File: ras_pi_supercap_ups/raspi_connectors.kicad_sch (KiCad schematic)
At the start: 2 parts

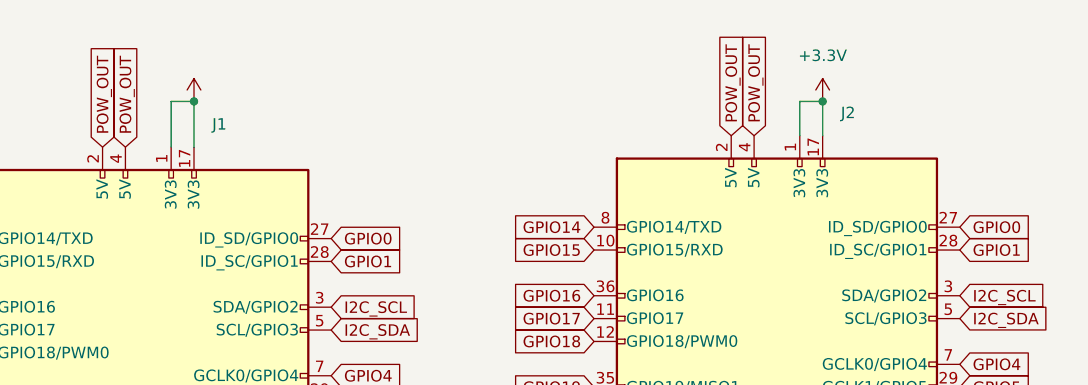
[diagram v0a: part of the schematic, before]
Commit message: added 3d model
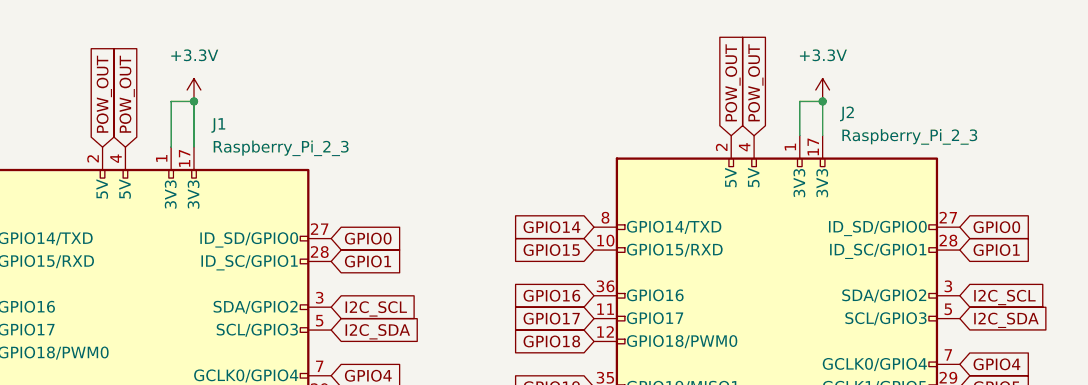
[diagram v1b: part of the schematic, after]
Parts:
- J1, J2: value (none) -> Raspberry_Pi_2_3
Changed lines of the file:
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@@
       (effects (font (size 1.27 1.27)) hide)
     )
-    (property "Value" "" (id 1) (at 66.04 21.59 0))
+    (property "Value" "+3.3V" (id 1) (at 66.04 21.59 0))
     (property "Footprint" "" (id 2) (at 66.04 26.67 0)
       (effects (font (size 1.27 1.27)) hide)
@@
       (effects (font (size 1.27 1.27)) (justify left))
     )
-    (property "Value" "" (id 1) (at 137.9094 30.48 0)
+    (property "Value" "Raspberry_Pi_2_3" (id 1) (at 137.9094 30.48 0)
       (effects (font (size 1.27 1.27)) (justify left))
     )
@@
       (effects (font (size 1.27 1.27)) (justify left))
     )
-    (property "Value" "" (id 1) (at 68.0594 31.75 0)
+    (property "Value" "Raspberry_Pi_2_3" (id 1) (at 68.0594 31.75 0)
       (effects (font (size 1.27 1.27)) (justify left))
     )

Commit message: As ordered v0.9
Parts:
- J1, J2: footprint (none) -> Connector_PinSocket_2.54mm:PinSocket_2x20_P2.54mm_Vertical; LCSC (none) -> DNP
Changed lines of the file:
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@@
   (junction (at 135.89 100.33) (diameter 0) (color 0 0 0 0)
   )
+  (junction (at 133.35 26.67) (diameter 0) (color 0 0 0 0)
+  )
   (junction (at 63.5 101.6) (diameter 0) (color 0 0 0 0)
   )
@@
     (stroke (width 0) (type default) (color 0 0 0 0))
   )
+  (wire (pts (xy 105.41 24.13) (xy 105.41 22.86))
+    (stroke (width 0) (type default) (color 0 0 0 0))
+  )
   (wire (pts (xy 55.88 101.6) (xy 58.42 101.6))
     (stroke (width 0) (type default) (color 0 0 0 0))
@@
     (stroke (width 0) (type default) (color 0 0 0 0))
   )
+  (wire (pts (xy 100.33 24.13) (xy 105.41 24.13))
+    (stroke (width 0) (type default) (color 0 0 0 0))
+  )
   (wire (pts (xy 123.19 100.33) (xy 125.73 100.33))
     (stroke (width 0) (type default) (color 0 0 0 0))
@@
     (property "Intersheet References" "${INTERSHEET_REFS}" (id 0) (at 91.3131 51.9906 0)
       (effects (font (size 1.27 1.27)) (justify left) hide)
+    )
+  )
+  (global_label "POW_OUT" (shape input) (at 100.33 24.13 180) (fields_autoplaced)
+    (effects (font (size 1.27 1.27)) (justify right))
+    (property "Intersheet References" "${INTERSHEET_REFS}" (id 0) (at 89.2688 24.2094 0)
+      (effects (font (size 1.27 1.27)) (justify right) hide)
     )
   )
@@
   )
   (symbol (lib_id "power:+3.3V") (at 135.89 26.67 0) (unit 1)
-    (in_bom yes) (on_board yes) (fields_autoplaced)
+    (in_bom yes) (on_board yes)
     (property "Reference" "#PWR035" (id 0) (at 135.89 30.48 0)
       (effects (font (size 1.27 1.27)) hide)
     )
-    (property "Value" "+3.3V" (id 1) (at 135.89 21.59 0))
+    (property "Value" "+3.3V" (id 1) (at 135.89 20.32 90))
     (property "Footprint" "" (id 2) (at 135.89 26.67 0)
       (effects (font (size 1.27 1.27)) hide)
@@
       (effects (font (size 1.27 1.27)) (justify left))
     )
-    (property "Footprint" "" (id 2) (at 130.81 63.5 0)
+    (property "Footprint" "Connector_PinSocket_2.54mm:PinSocket_2x20_P2.54mm_Vertical" (id 2) (at 130.81 63.5 0)
       (effects (font (size 1.27 1.27)) hide)
     )
     (property "Datasheet" "https://www.raspberrypi.org/documentation/hardware/raspberrypi/schematics/rpi_SCH_3bplus_1p0_reduced.pdf" (id 3) (at 130.81 63.5 0)
+      (effects (font (size 1.27 1.27)) hide)
+    )
+    (property "LCSC" "DNP" (id 4) (at 130.81 63.5 0)
       (effects (font (size 1.27 1.27)) hide)
     )
@@
     (pin "9")
   )
+  (symbol (lib_id "power:PWR_FLAG") (at 133.35 26.67 0) (unit 1)
+    (in_bom yes) (on_board yes)
+    (property "Reference" "#FLG0101" (id 0) (at 133.35 24.765 0)
+      (effects (font (size 1.27 1.27)) hide)
+    )
+    (property "Value" "PWR_FLAG" (id 1) (at 133.35 19.05 90))
+    (property "Footprint" "" (id 2) (at 133.35 26.67 0)
+      (effects (font (size 1.27 1.27)) hide)
+    )
+    (property "Datasheet" "~" (id 3) (at 133.35 26.67 0)
+      (effects (font (size 1.27 1.27)) hide)
+    )
+    (pin "1")
+  )
+  (symbol (lib_id "power:PWR_FLAG") (at 105.41 22.86 0) (unit 1)
+    (in_bom yes) (on_board yes)
+    (property "Reference" "#FLG0102" (id 0) (at 105.41 20.955 0)
+      (effects (font (size 1.27 1.27)) hide)
+    )
+    (property "Value" "PWR_FLAG" (id 1) (at 105.41 19.05 0))
+    (property "Footprint" "" (id 2) (at 105.41 22.86 0)
+      (effects (font (size 1.27 1.27)) hide)
+    )
+    (property "Datasheet" "~" (id 3) (at 105.41 22.86 0)
+      (effects (font (size 1.27 1.27)) hide)
+    )
+    (pin "1")
+  )
   (symbol (lib_id "Connector:Raspberry_Pi_2_3") (at 60.96 64.77 0) (unit 1)
     (in_bom yes) (on_board yes) (fields_autoplaced)
@@
       (effects (font (size 1.27 1.27)) (justify left))
     )
-    (property "Footprint" "" (id 2) (at 60.96 64.77 0)
+    (property "Footprint" "Connector_PinSocket_2.54mm:PinSocket_2x20_P2.54mm_Vertical" (id 2) (at 60.96 64.77 0)
       (effects (font (size 1.27 1.27)) hide)
     )
@@
       (effects (font (size 1.27 1.27)) hide)
     )
+    (property "LCSC" "DNP" (id 4) (at 60.96 64.77 0)
+      (effects (font (size 1.27 1.27)) hide)
+    )
